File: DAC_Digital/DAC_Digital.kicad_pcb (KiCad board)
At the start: 2 copper layers, 100 x 100 mm, 131 parts, among them J1 +5V_in, J10 USB_Dev4, J11 P9, J12 Anlg_in, J13 Anlg_I2C, J14 P8, J15 Test, J16 Test, J17 Fix, J18 Fix, J19 Fix, J2 DBG_PORT, J20 Fix, J3 DSPL_PORT, J4 Out_SPDIF, J5 USB0, J6 USB1, J7 USB_Dev1, J8 USB_Dev2, J9 USB_Dev3, Q1 2n7002, Q2 2N7002, Q3 FDS4435, Q4 FDS4435, Q5 2N7002, Q6 2N7002, T1 DA103C, U1 CS8406_2, U2 PIC18F6722, U3 74LVC1G08GW, U4 PCM2903C, U5 74LVC1G08GW, U6 USB2514B-AEZC, U7 NE5532, X1 7A-24.000MAAJ-T, Y1 10MHz, Y2 12MHz

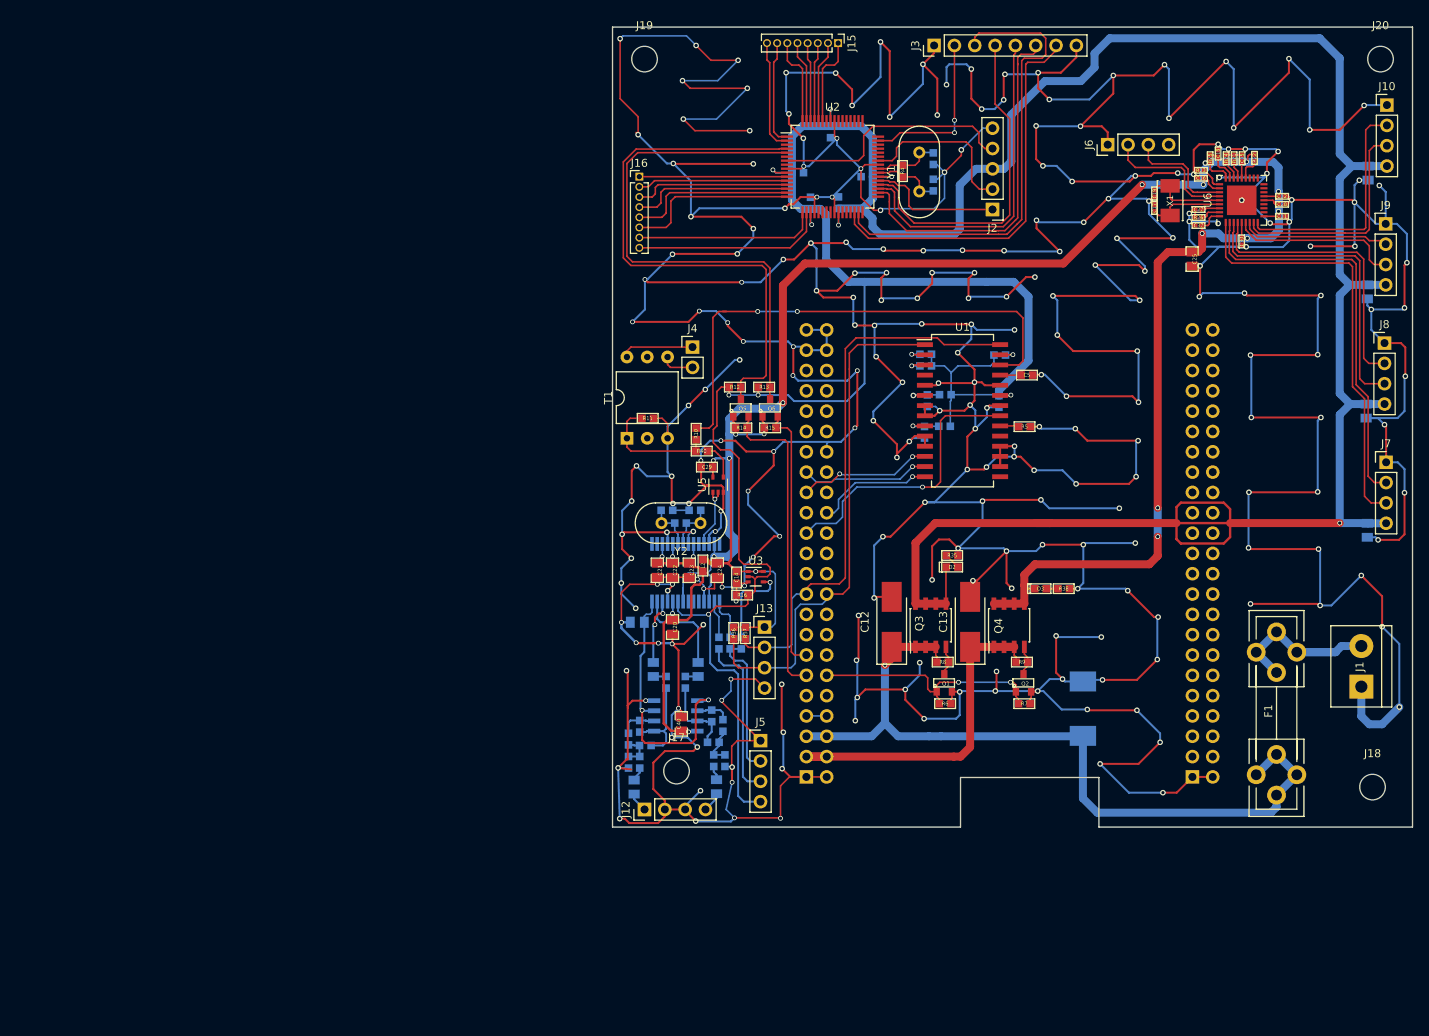
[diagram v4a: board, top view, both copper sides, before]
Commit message: Update layout DAC_Digital
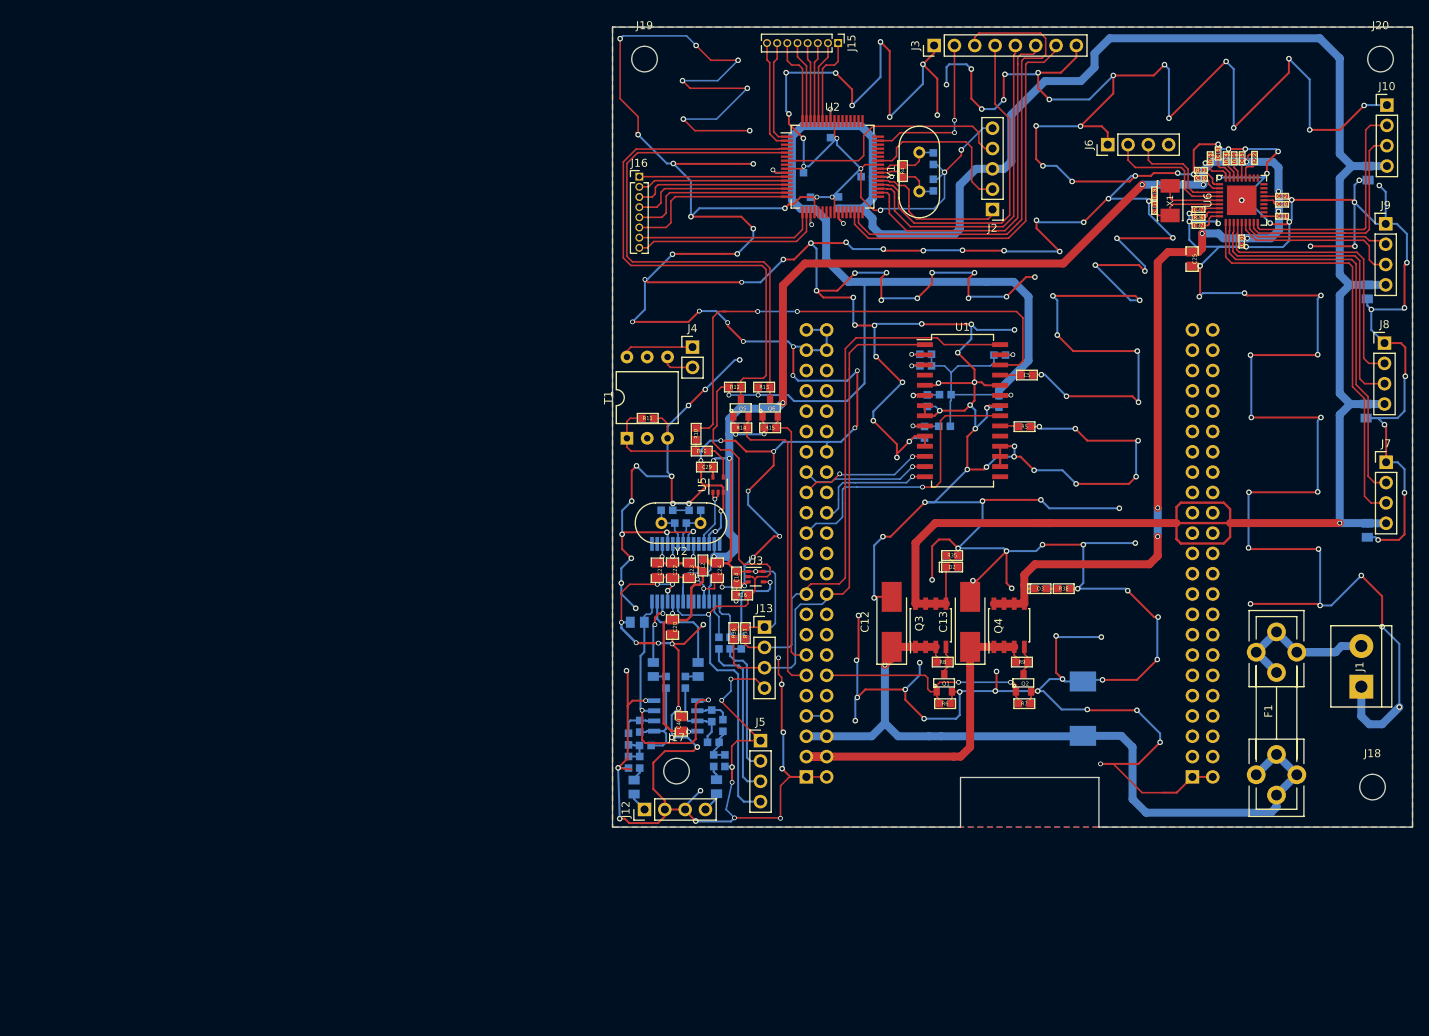
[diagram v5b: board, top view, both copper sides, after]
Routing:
- net GND: track 1709.7 -> 1713.2 mm
- net Net-(J2-Pad1): track 17.0 -> 18.8 mm
- net /DATA: track 14.8 -> 15.7 mm
- net /GPIO_117: track 35.9 -> 36.8 mm
- net /VDD_5V: track 98.6 -> 97.9 mm
- added copper zone on B.Cu, net GND
- added copper zone on F.Cu, net GND

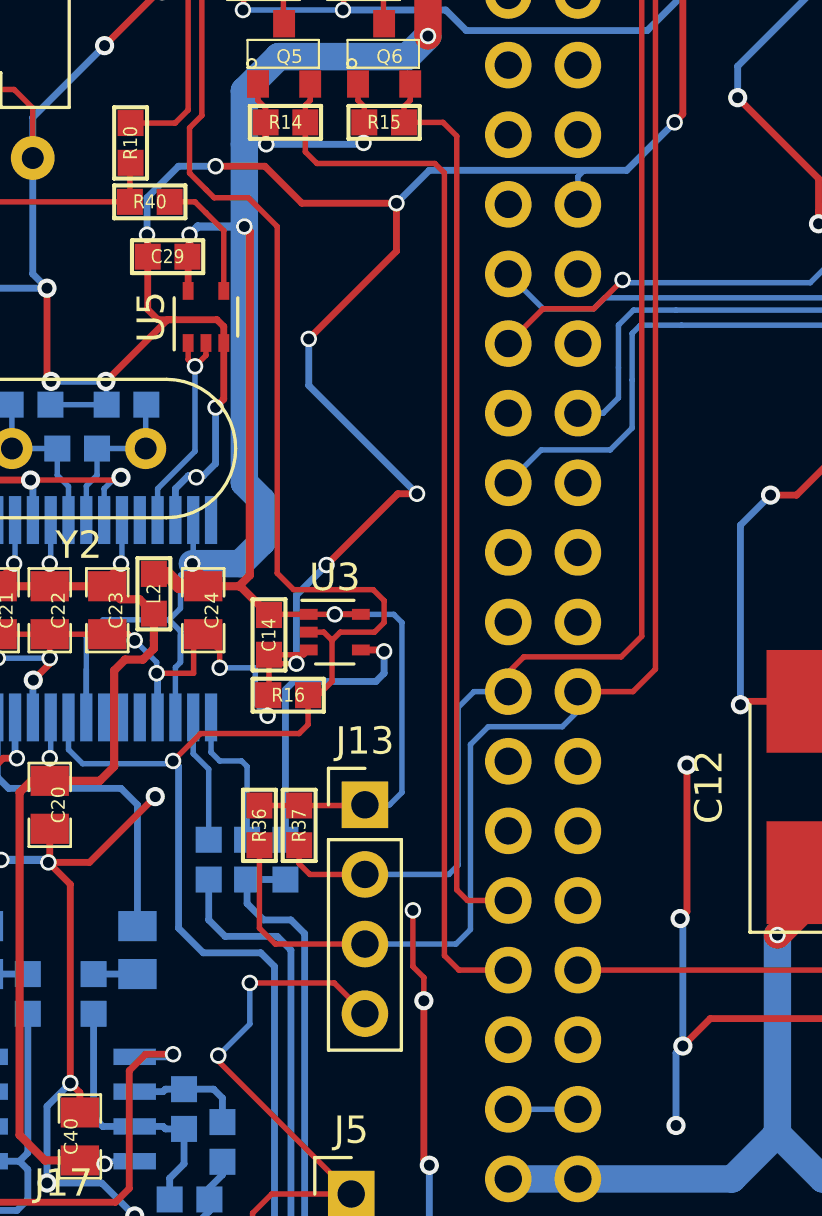
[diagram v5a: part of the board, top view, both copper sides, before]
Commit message: Place cmp DAC_Analog
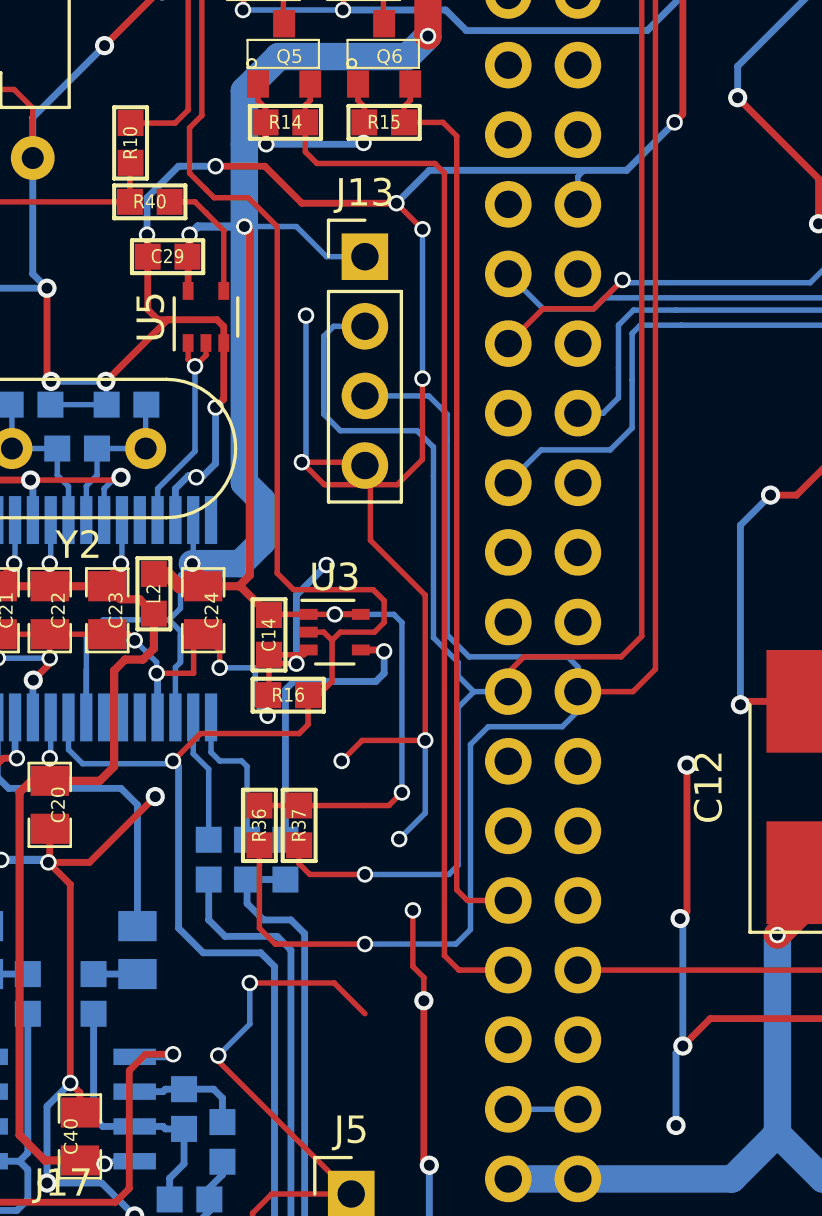
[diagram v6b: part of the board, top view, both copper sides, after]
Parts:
- moved J13 20.0 mm to (114.0, 119.0)
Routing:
- net GND: track 1713.2 -> 1735.4 mm, vias 259 -> 264
- net /I2C2_SCL: track 69.6 -> 88.2 mm, vias 0 -> 1
- net /I2C2_SDA: track 65.4 -> 82.9 mm, vias 0 -> 1
- net VCC: track 296.0 -> 300.8 mm, vias 17 -> 18

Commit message: Update layout
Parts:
- moved D2 74.1 mm to (183.6, 73.5), turned to 0 degrees
- moved R35 71.1 mm to (180.6, 73.5), turned to 180 degrees
- moved R38 61.0 mm to (181.4, 81.1), turned to 90 degrees
- moved D3 60.3 mm to (180.7, 83.2)
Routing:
- net GND: track 1735.4 -> 1745.5 mm, vias 264 -> 266
- net /+5v_Dev: track 494.8 -> 492.0 mm, vias 10 -> 11
- net VCC: track 300.8 -> 302.2 mm
- net Net-(D2-Pad1): track 2.05 -> 1.50 mm
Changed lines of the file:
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@@
     (thickness 1.6)
     (drawings 2780)
-    (tracks 2194)
+    (tracks 2207)
     (zones 0)
     (modules 131)
@@
   )
   (module Yame_library:SM0603-LED-MR placed (layer F.Cu)
-    (at 137.45 131.5 180)
+    (at 183.55 73.5)
     (attr smd)
-    (fp_text reference D2 (at 0 0 180) (layer F.SilkS)
+    (fp_text reference D2 (at 0 0) (layer F.SilkS)
       (effects (font (size 0.508 0.4572) (thickness 0.1143)))
     )
-    (fp_text value LED (at 0 0 180) (layer F.SilkS) hide
+    (fp_text value LED (at 0 0) (layer F.SilkS) hide
       (effects (font (size 0.508 0.4572) (thickness 0.1143)))
     )
@@
     (fp_line (start -1.3 0.6) (end 1.3 0.6) (layer F.SilkS) (width 0.15))
     (fp_line (start 1.3 0.6) (end 1.3 -0.6) (layer F.SilkS) (width 0.15))
-    (pad 1 smd rect (at -0.725 0 180) (size 0.95 0.95) (layers F.Cu F.Paste F.Mask)
+    (pad 1 smd rect (at -0.725 0) (size 0.95 0.95) (layers F.Cu F.Paste F.Mask)
       (net 32 "Net-(D2-Pad1)"))
-    (pad 2 smd rect (at 0.725 0 180) (size 0.95 0.95) (layers F.Cu F.Paste F.Mask)
+    (pad 2 smd rect (at 0.725 0) (size 0.95 0.95) (layers F.Cu F.Paste F.Mask)
       (net 1 /+5v_Dev))
     (model smd\resistors\R0603.wrl
@@
   )
   (module Yame_library:SM0603-LED-MR placed (layer F.Cu)
-    (at 148.5 134.2 180)
+    (at 180.7 83.2 180)
     (attr smd)
     (fp_text reference D3 (at 0 0 180) (layer F.SilkS)
@@
   )
   (module Yame_library:SM0603-MR placed (layer F.Cu)
-    (at 137.45 130.05)
+    (at 180.6 73.5 180)
     (attr smd)
-    (fp_text reference R35 (at 0 0) (layer F.SilkS)
+    (fp_text reference R35 (at 0 0 180) (layer F.SilkS)
       (effects (font (size 0.508 0.4572) (thickness 0.1143)))
     )
-    (fp_text value 1k (at 0 0) (layer F.SilkS) hide
+    (fp_text value 1k (at 0 0 180) (layer F.SilkS) hide
       (effects (font (size 0.508 0.4572) (thickness 0.1143)))
     )
@@
     (fp_line (start -1.3 0.6) (end 1.3 0.6) (layer F.SilkS) (width 0.15))
     (fp_line (start 1.3 0.6) (end 1.3 -0.6) (layer F.SilkS) (width 0.15))
-    (pad 1 smd rect (at -0.725 0) (size 0.95 0.95) (layers F.Cu F.Paste F.Mask)
+    (pad 1 smd rect (at -0.725 0 180) (size 0.95 0.95) (layers F.Cu F.Paste F.Mask)
       (net 32 "Net-(D2-Pad1)"))
-    (pad 2 smd rect (at 0.725 0) (size 0.95 0.95) (layers F.Cu F.Paste F.Mask)
+    (pad 2 smd rect (at 0.725 0 180) (size 0.95 0.95) (layers F.Cu F.Paste F.Mask)
       (net 2 GND))
     (model smd\resistors\R0603.wrl
@@
   )
   (module Yame_library:SM0603-MR placed (layer F.Cu)
-    (at 151.4 134.2)
+    (at 181.4 81.1 90)
     (attr smd)
-    (fp_text reference R38 (at 0 0) (layer F.SilkS)
+    (fp_text reference R38 (at 0 0 90) (layer F.SilkS)
       (effects (font (size 0.508 0.4572) (thickness 0.1143)))
     )
-    (fp_text value 1k (at 0 0) (layer F.SilkS) hide
+    (fp_text value 1k (at 0 0 90) (layer F.SilkS) hide
       (effects (font (size 0.508 0.4572) (thickness 0.1143)))
     )
@@
     (fp_line (start -1.3 0.6) (end 1.3 0.6) (layer F.SilkS) (width 0.15))
     (fp_line (start 1.3 0.6) (end 1.3 -0.6) (layer F.SilkS) (width 0.15))
-    (pad 1 smd rect (at -0.725 0) (size 0.95 0.95) (layers F.Cu F.Paste F.Mask)
+    (pad 1 smd rect (at -0.725 0 90) (size 0.95 0.95) (layers F.Cu F.Paste F.Mask)
       (net 33 "Net-(D3-Pad1)"))
-    (pad 2 smd rect (at 0.725 0) (size 0.95 0.95) (layers F.Cu F.Paste F.Mask)
+    (pad 2 smd rect (at 0.725 0 90) (size 0.95 0.95) (layers F.Cu F.Paste F.Mask)
       (net 2 GND))
     (model smd\resistors\R0603.wrl
@@
   (gr_line (start 195 64) (end 195 164) (angle 90) (layer Edge.Cuts) (width 0.15))
   (gr_line (start 95 64) (end 195 64) (angle 90) (layer Edge.Cuts) (width 0.15))
+  (segment (start 184.275 73.5) (end 185.9 73.5) (width 0.2) (layer F.Cu) (net 1) (status 400000))
+  (segment (start 185.9 73.5) (end 185.9 73.7) (width 0.2) (layer B.Cu) (net 1))
+  (via (at 185.9 73.5) (size 0.6) (drill 0.4) (layers F.Cu B.Cu) (net 1))
   (segment (start 123.25 87.15) (end 123.25 87.95) (width 0.2) (layer F.Cu) (net 1))
   (segment (start 123.25 87.95) (end 123.25 86.675) (width 0.2) (layer B.Cu) (net 1))
@@
   (segment (start 183.4 65.4) (end 157.15 65.4) (width 1) (layer B.Cu) (net 1))
   (segment (start 185.9 67.9) (end 183.4 65.4) (width 1) (layer B.Cu) (net 1))
-  (segment (start 185.9 79.85) (end 185.9 67.9) (width 1) (layer B.Cu) (net 1))
+  (segment (start 185.9 79.85) (end 185.9 73.7) (width 1) (layer B.Cu) (net 1))
+  (segment (start 185.9 73.7) (end 185.9 67.9) (width 1) (layer B.Cu) (net 1))
   (segment (start 189.2 111.125) (end 191.495 111.125) (width 1) (layer B.Cu) (net 1))
   (segment (start 191.495 111.125) (end 191.5 111.12) (width 1) (layer B.Cu) (net 1))
@@
   (segment (start 189.35 126.025) (end 191.695 126.025) (width 1) (layer B.Cu) (net 1))
   (segment (start 191.695 126.025) (end 191.7 126.02) (width 1) (layer B.Cu) (net 1))
-  (segment (start 136.68 136.075) (end 136.68 131.545) (width 0.2) (layer F.Cu) (net 1))
-  (segment (start 136.68 131.545) (end 136.725 131.5) (width 0.2) (layer F.Cu) (net 1))
   (segment (start 135.41 136.075) (end 136.68 136.075) (width 1) (layer F.Cu) (net 1))
   (segment (start 134.14 136.075) (end 135.41 136.075) (width 1) (layer F.Cu) (net 1))
@@
   (segment (start 112.8 133) (end 112.5 132.7) (width 0.2) (layer F.Cu) (net 1))
   (segment (start 112.5 132.7) (end 111.95 132.7) (width 0.2) (layer F.Cu) (net 1))
+  (segment (start 179.875 73.5) (end 178.9 73.5) (width 0.2) (layer F.Cu) (net 2) (status 400000))
+  (segment (start 178.4 69.1) (end 179.55 67.95) (width 0.2) (layer B.Cu) (net 2))
+  (segment (start 178.4 73) (end 178.4 69.1) (width 0.2) (layer B.Cu) (net 2))
+  (segment (start 178.9 73.5) (end 178.4 73) (width 0.2) (layer B.Cu) (net 2))
+  (via (at 178.9 73.5) (size 0.6) (drill 0.4) (layers F.Cu B.Cu) (net 2))
+  (segment (start 181.4 80.375) (end 181.4 79.2) (width 0.2) (layer F.Cu) (net 2) (status 400000))
+  (segment (start 182.15 78.45) (end 182.15 76.85) (width 0.2) (layer B.Cu) (net 2))
+  (segment (start 181.5 79.1) (end 182.15 78.45) (width 0.2) (layer B.Cu) (net 2))
+  (via (at 181.5 79.1) (size 0.6) (drill 0.4) (layers F.Cu B.Cu) (net 2))
+  (segment (start 181.4 79.2) (end 181.5 79.1) (width 0.2) (layer F.Cu) (net 2))
   (segment (start 111.7 126.5) (end 113.88 126.5) (width 0.2) (layer F.Cu) (net 2))
   (segment (start 113.88 126.5) (end 114 126.62) (width 0.2) (layer F.Cu) (net 2))
@@
   (segment (start 153.85 128.7) (end 153.85 133.5) (width 0.25) (layer B.Cu) (net 2))
   (segment (start 153.85 133.5) (end 153.15 134.2) (width 0.25) (layer B.Cu) (net 2))
-  (segment (start 153.15 134.2) (end 152.125 134.2) (width 0.25) (layer F.Cu) (net 2))
   (via (at 153.15 134.2) (size 0.7) (drill 0.4) (layers F.Cu B.Cu) (net 2))
   (segment (start 144.25 129.5) (end 147.95 129.5) (width 0.25) (layer B.Cu) (net 2))
@@
   (segment (start 145.45 142.75) (end 145.45 143.375) (width 0.2) (layer F.Cu) (net 8))
   (segment (start 145.21 142.51) (end 145.45 142.75) (width 0.2) (layer F.Cu) (net 8))
+  (segment (start 179.975 83.2) (end 178.7 83.2) (width 0.2) (layer F.Cu) (net 9))
+  (segment (start 178.25 83.65) (end 178.25 84.55) (width 0.2) (layer F.Cu) (net 9))
+  (segment (start 178.7 83.2) (end 178.25 83.65) (width 0.2) (layer F.Cu) (net 9))
   (segment (start 111 117.9) (end 111.5 117.9) (width 0.2) (layer B.Cu) (net 9))
   (segment (start 109.6 117.9) (end 111 117.9) (width 0.2) (layer B.Cu) (net 9))
@@
   (segment (start 143.94 136.075) (end 145.21 136.075) (width 0.2) (layer F.Cu) (net 9))
   (segment (start 142.67 136.075) (end 143.94 136.075) (width 0.2) (layer F.Cu) (net 9))
-  (segment (start 147.775 134.2) (end 146.91 134.2) (width 0.25) (layer F.Cu) (net 9))
-  (segment (start 146.91 134.2) (end 146.48 133.77) (width 0.25) (layer F.Cu) (net 9))
   (segment (start 178.275 87.65) (end 178.275 87.075) (width 0.25) (layer F.Cu) (net 9))
   (segment (start 178.3 87.1) (end 178.3 87.5) (width 0.25) (layer B.Cu) (net 9))
@@
   (segment (start 107.65 157.1) (end 107.65 156.425) (width 0.25) (layer B.Cu) (net 31))
   (segment (start 108 157.45) (end 107.65 157.1) (width 0.25) (layer B.Cu) (net 31))
-  (segment (start 136.725 130.05) (end 138.175 131.5) (width 0.2) (layer F.Cu) (net 32))
-  (segment (start 149.225 134.2) (end 150.675 134.2) (width 0.25) (layer F.Cu) (net 33))
+  (segment (start 182.825 73.5) (end 181.325 73.5) (width 0.2) (layer F.Cu) (net 32) (status C00000))
+  (segment (start 181.425 83.2) (end 181.425 81.85) (width 0.2) (layer F.Cu) (net 33) (status C00000))
+  (segment (start 181.425 81.85) (end 181.4 81.825) (width 0.2) (layer F.Cu) (net 33) (status C00000))
   (segment (start 180.54 142.14) (end 185.36 142.14) (width 1) (layer B.Cu) (net 34))
   (segment (start 186.13 141.37) (end 188.6 141.37) (width 1) (layer B.Cu) (net 34))
